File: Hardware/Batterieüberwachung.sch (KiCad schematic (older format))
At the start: 7 parts, among them Q1 BC847B_215

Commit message: Martin ist unförmig
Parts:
- Q301: renamed from Q1; value BC847B_215 -> BC847B_215-dk_Transistors-Bipolar-BJT-Single
- gave numbers to parts that had none: 4
- renumbered R4 to R301, R5 to R302
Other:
- moved on the sheet: C301, C302, R301, R302, R303, R304

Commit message: Ich hoffe wir koennen jetzt den Master mergen!
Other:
- note added: "MOSFET statt Bipolar"
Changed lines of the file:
@@
 	7400 4600 7100 4600
 Connection ~ 7100 4600
+Text Notes 5750 3700 0    20   ~ 4
+MOSFET statt Bipolar
 $EndSCHEMATC

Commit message: Zwischenspeicher Arbeit OTH
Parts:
- removed Q301: BC847B_215-dk_Transistors-Bipolar-BJT-Single, digikey-footprints:SOT-23-3, symbol E-Ink-rescue:BC847B_215-dk_Transistors-Bipolar-BJT-Single
- added Q301: 2N7000, digikey-footprints:TO-92-3, symbol E-Ink:2N7000
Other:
- note removed: "MOSFET statt Bipolar"
- moved on the sheet: R301
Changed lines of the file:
@@
 EESchema Schematic File Version 4
-EELAYER 30 0
+LIBS:E-Ink-cache
+EELAYER 29 0
 EELAYER END
 $Descr A4 11693 8268
@@
 $EndDescr
 $Comp
-L E-Ink-rescue:BC847B_215-dk_Transistors-Bipolar-BJT-Single Q?
-U 1 1 5DE4FE79
-P 5600 3900
-AR Path="/5DE4FE79" Ref="Q?"  Part="1"
-AR Path="/5DE4BC0A/5DE4FE79" Ref="Q301"  Part="1"
-F 0 "Q301" V 5827 4032 60  0000 C CNN
-F 1 "BC847B_215-dk_Transistors-Bipolar-BJT-Single" V 5906 3689 60  0001 C CNN
-F 2 "digikey-footprints:SOT-23-3" H 5800 4100 60  0001 L CNN
-F 3 "https://assets.nexperia.com/documents/data-sheet/BC847_SER.pdf" H 5800 4200 60  0001 L CNN
-F 4 "1727-2921-1-ND" H 5800 4300 60  0001 L CNN "Digi-Key_PN"
-F 5 "BC847B,215" H 5800 4400 60  0001 L CNN "MPN"
-F 6 "Discrete Semiconductor Products" H 5800 4500 60  0001 L CNN "Category"
-F 7 "Transistors - Bipolar (BJT) - Single" H 5800 4600 60  0001 L CNN "Family"
-F 8 "https://assets.nexperia.com/documents/data-sheet/BC847_SER.pdf" H 5800 4700 60  0001 L CNN "DK_Datasheet_Link"
-F 9 "/product-detail/en/nexperia-usa-inc/BC847B,215/1727-2921-1-ND/763460" H 5800 4800 60  0001 L CNN "DK_Detail_Page"
-F 10 "TRANS NPN 45V 0.1A SOT23" H 5800 4900 60  0001 L CNN "Description"
-F 11 "Nexperia USA Inc." H 5800 5000 60  0001 L CNN "Manufacturer"
-F 12 "Active" H 5800 5100 60  0001 L CNN "Status"
-	1    5600 3900
-	0    -1   -1   0
-$EndComp
-$Comp
 L power:GND #PWR?
 U 1 1 5DE4FE7F
@@
 	0    1    1    0
 $EndComp
-$Comp
-L E-Ink:4k7 R?
-U 1 1 5DE4FE8B
-P 5650 4300
-AR Path="/5DE4FE8B" Ref="R?"  Part="1"
-AR Path="/5DE4BC0A/5DE4FE8B" Ref="R301"  Part="1"
-F 0 "R301" V 5704 4328 50  0000 L CNN
-F 1 "4k7" V 5795 4328 50  0000 L CNN
-F 2 "Resistor_SMD:R_0805_2012Metric_Pad1.15x1.40mm_HandSolder" H 5700 4150 50  0001 C CNN
-F 3 "" H 5650 4350 50  0001 C CNN
-	1    5650 4300
-	0    1    1    0
-$EndComp
-Wire Wire Line
-	6100 4200 5600 4200
-Wire Wire Line
-	5600 4100 5600 4200
-Connection ~ 5600 4200
 Wire Wire Line
 	6100 3800 5800 3800
@@
 Wire Wire Line
 	3950 3950 3900 3950
-Wire Wire Line
-	5500 4600 5600 4600
 Text HLabel 3900 4100 0    50   Output ~ 10
 GPIO_Vmess
@@
 	7400 4600 7100 4600
 Connection ~ 7100 4600
-Text Notes 5750 3700 0    20   ~ 4
-MOSFET statt Bipolar
+Wire Wire Line
+	6100 4200 5700 4200
+$Comp
+L E-Ink:4k7 R?
+U 1 1 5DE4FE8B
+P 5750 4300
+AR Path="/5DE4FE8B" Ref="R?"  Part="1"
+AR Path="/5DE4BC0A/5DE4FE8B" Ref="R301"  Part="1"
+F 0 "R301" V 5804 4328 50  0000 L CNN
+F 1 "4k7" V 5895 4328 50  0000 L CNN
+F 2 "Resistor_SMD:R_0805_2012Metric_Pad1.15x1.40mm_HandSolder" H 5800 4150 50  0001 C CNN
+F 3 "" H 5750 4350 50  0001 C CNN
+	1    5750 4300
+	0    1    1    0
+$EndComp
+$Comp
+L E-Ink:2N7000 Q301
+U 1 1 5DF417CB
+P 5600 3800
+F 0 "Q301" V 5867 3800 60  0000 C CNN
+F 1 "2N7000" V 5761 3800 60  0000 C CNN
+F 2 "digikey-footprints:TO-92-3" H 5800 4000 60  0001 L CNN
+F 3 "https://www.onsemi.com/pub/Collateral/NDS7002A-D.PDF" H 5800 4100 60  0001 L CNN
+F 4 "2N7000FS-ND" H 5800 4200 60  0001 L CNN "Digi-Key_PN"
+F 5 "2N7000" H 5800 4300 60  0001 L CNN "MPN"
+F 6 "Discrete Semiconductor Products" H 5800 4400 60  0001 L CNN "Category"
+F 7 "Transistors - FETs, MOSFETs - Single" H 5800 4500 60  0001 L CNN "Family"
+F 8 "https://www.onsemi.com/pub/Collateral/NDS7002A-D.PDF" H 5800 4600 60  0001 L CNN "DK_Datasheet_Link"
+F 9 "/product-detail/en/on-semiconductor/2N7000/2N7000FS-ND/244278" H 5800 4700 60  0001 L CNN "DK_Detail_Page"
+F 10 "MOSFET N-CH 60V 200MA TO-92" H 5800 4800 60  0001 L CNN "Description"
+F 11 "ON Semiconductor" H 5800 4900 60  0001 L CNN "Manufacturer"
+F 12 "Active" H 5800 5000 60  0001 L CNN "Status"
+	1    5600 3800
+	0    -1   -1   0
+$EndComp
+Wire Wire Line
+	5700 4100 5700 4200
+Connection ~ 5700 4200
+Wire Wire Line
+	5500 4600 5700 4600
 $EndSCHEMATC

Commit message: save work at arges, finished layout and routing
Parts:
- Q301: footprint digikey-footprints:TO-92-3 -> Digikey:TO-92-3
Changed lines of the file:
@@
 EESchema Schematic File Version 4
 LIBS:E-Ink-cache
-EELAYER 29 0
+EELAYER 30 0
 EELAYER END
 $Descr A4 11693 8268
@@
 F 0 "Q301" V 5867 3800 60  0000 C CNN
 F 1 "2N7000" V 5761 3800 60  0000 C CNN
-F 2 "digikey-footprints:TO-92-3" H 5800 4000 60  0001 L CNN
+F 2 "Digikey:TO-92-3" H 5800 4000 60  0001 L CNN
 F 3 "https://www.onsemi.com/pub/Collateral/NDS7002A-D.PDF" H 5800 4100 60  0001 L CNN
 F 4 "2N7000FS-ND" H 5800 4200 60  0001 L CNN "Digi-Key_PN"

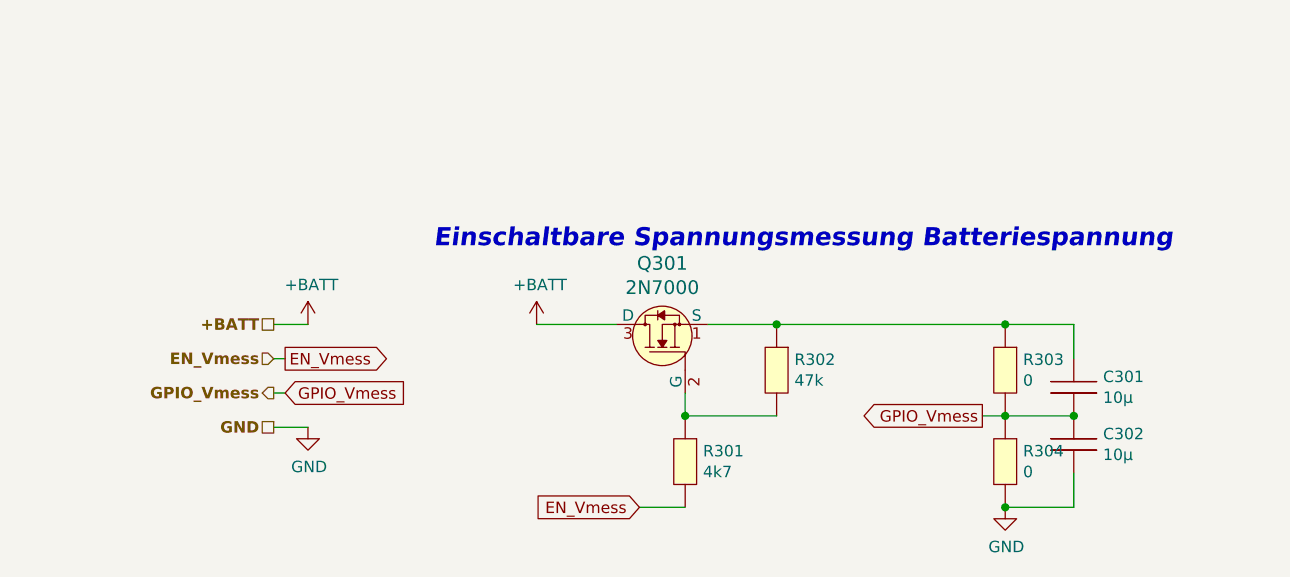
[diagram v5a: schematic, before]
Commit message: Added new MCU and redesigned schematics
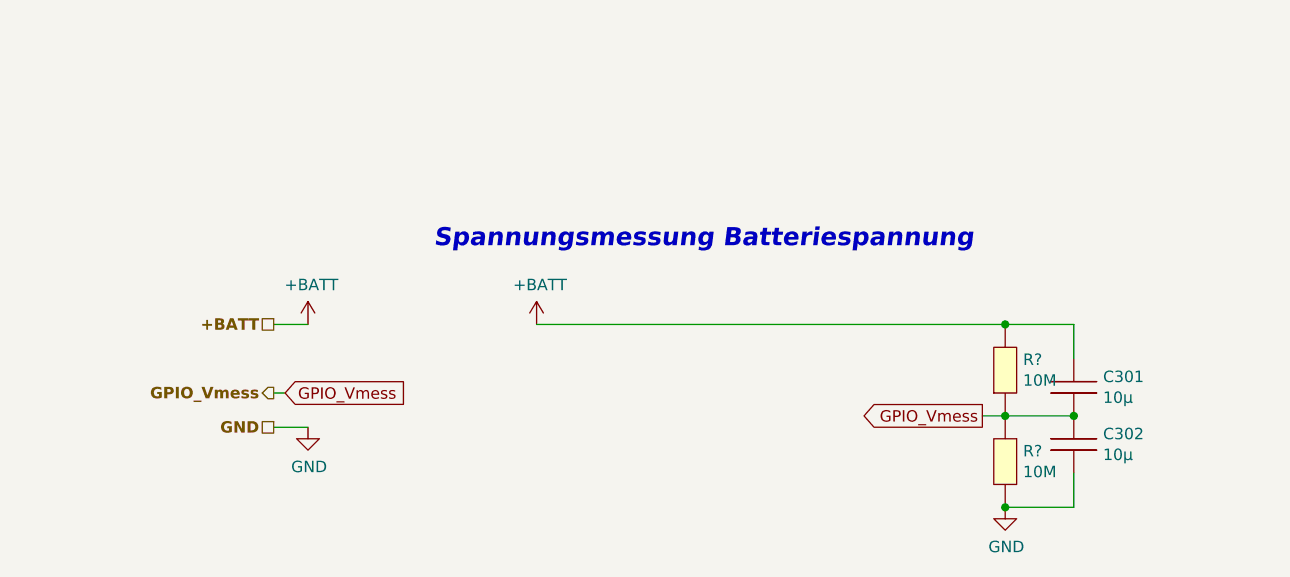
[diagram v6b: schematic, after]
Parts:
- removed Q301: 2N7000, Digikey:TO-92-3, symbol E-Ink:2N7000
- removed R301: 4k7, Resistor_SMD:R_0805_2012Metric_Pad1.15x1.40mm_HandSolder, symbol E-Ink:4k7
- removed R302: 47k, Resistor_SMD:R_0805_2012Metric_Pad1.15x1.40mm_HandSolder, symbol E-Ink:47k
- removed R303, R304: 0, Resistor_SMD:R_0805_2012Metric_Pad1.15x1.40mm_HandSolder, symbol E-Ink:0
- added R? (x2): 10M, Resistor_SMD:R_0805_2012Metric_Pad1.15x1.40mm_HandSolder, symbol E-Ink:10M
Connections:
- net +BATT: now also C301.1, R?.2
- net GND: now also R?.2
- net GPIO_Vmess: now also R?.1, R?.1
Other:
- note added: "Spannungsmessung Batteriespannung\n\n"
- note removed: "Einschaltbare Spannungsmessung Batteriespannung\n\n"
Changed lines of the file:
@@
 EESchema Schematic File Version 4
-LIBS:E-Ink-cache
 EELAYER 30 0
 EELAYER END
@@
 	1    0    0    -1
 $EndComp
-$Comp
-L E-Ink:47k R?
-U 1 1 5DE4FE85
-P 6150 3900
-AR Path="/5DE4FE85" Ref="R?"  Part="1"
-AR Path="/5DE4BC0A/5DE4FE85" Ref="R302"  Part="1"
-F 0 "R302" V 6204 3928 50  0000 L CNN
-F 1 "47k" V 6295 3928 50  0000 L CNN
-F 2 "Resistor_SMD:R_0805_2012Metric_Pad1.15x1.40mm_HandSolder" H 6200 3750 50  0001 C CNN
-F 3 "" H 6150 3950 50  0001 C CNN
-	1    6150 3900
-	0    1    1    0
-$EndComp
-Wire Wire Line
-	6100 3800 5800 3800
-Connection ~ 6100 3800
 Text GLabel 7000 4200 0    50   Output ~ 0
 GPIO_Vmess
-Wire Wire Line
-	6100 3800 7100 3800
-Text GLabel 5500 4600 0    50   Input ~ 0
-EN_Vmess
 $Comp
 L power:+BATT #PWR?
@@
 	1    0    0    -1
 $EndComp
-Wire Wire Line
-	5050 3800 5400 3800
 Text Notes 4600 3600 0    79   Italic 16
-Einschaltbare Spannungsmessung Batteriespannung\n\n
-Text HLabel 3900 3950 0    50   Input ~ 10
-EN_Vmess
+Spannungsmessung Batteriespannung\n\n
 Text HLabel 3900 3800 0    50   UnSpc ~ 10
 +BATT
@@
 Wire Wire Line
 	4050 3800 3900 3800
-Text GLabel 3950 3950 2    50   Output ~ 0
-EN_Vmess
-Wire Wire Line
-	3950 3950 3900 3950
 Text HLabel 3900 4100 0    50   Output ~ 10
 GPIO_Vmess
@@
 	4050 4250 3900 4250
 $Comp
-L E-Ink:0 R303
-U 1 1 5DEEEA28
-P 7150 3900
-F 0 "R303" V 7204 3928 50  0000 L CNN
-F 1 "0" V 7295 3928 50  0000 L CNN
-F 2 "Resistor_SMD:R_0805_2012Metric_Pad1.15x1.40mm_HandSolder" H 7200 3750 50  0001 C CNN
-F 3 "" H 7150 3950 50  0001 C CNN
-	1    7150 3900
-	0    1    1    0
-$EndComp
-$Comp
-L E-Ink:0 R304
-U 1 1 5DEEF0E3
-P 7150 4300
-F 0 "R304" V 7204 4328 50  0000 L CNN
-F 1 "0" V 7295 4328 50  0000 L CNN
-F 2 "Resistor_SMD:R_0805_2012Metric_Pad1.15x1.40mm_HandSolder" H 7200 4150 50  0001 C CNN
-F 3 "" H 7150 4350 50  0001 C CNN
-	1    7150 4300
-	0    1    1    0
-$EndComp
-Wire Wire Line
-	7000 4200 7100 4200
-Connection ~ 7100 4200
-$Comp
 L E-Ink:10µ C301
 U 1 1 5DEF06A2
@@
 	0    1    1    0
 $EndComp
-Wire Wire Line
-	7400 4200 7100 4200
 Connection ~ 7400 4200
 Wire Wire Line
 	7400 3950 7400 3800
 Wire Wire Line
-	7400 3800 7100 3800
-Connection ~ 7100 3800
-Wire Wire Line
 	7400 4450 7400 4600
 Wire Wire Line
 	7400 4600 7100 4600
-Connection ~ 7100 4600
 Wire Wire Line
-	6100 4200 5700 4200
+	5050 3800 7100 3800
+Wire Wire Line
+	7000 4200 7100 4200
 $Comp
-L E-Ink:4k7 R?
-U 1 1 5DE4FE8B
-P 5750 4300
-AR Path="/5DE4FE8B" Ref="R?"  Part="1"
-AR Path="/5DE4BC0A/5DE4FE8B" Ref="R301"  Part="1"
-F 0 "R301" V 5804 4328 50  0000 L CNN
-F 1 "4k7" V 5895 4328 50  0000 L CNN
-F 2 "Resistor_SMD:R_0805_2012Metric_Pad1.15x1.40mm_HandSolder" H 5800 4150 50  0001 C CNN
-F 3 "" H 5750 4350 50  0001 C CNN
-	1    5750 4300
+L E-Ink:10M R?
+U 1 1 5F96A47F
+P 7000 4000
+F 0 "R?" V 7046 3822 50  0000 R CNN
+F 1 "10M" V 6955 3822 50  0000 R CNN
+F 2 "Resistor_SMD:R_0805_2012Metric_Pad1.15x1.40mm_HandSolder" H 6900 3800 50  0001 C CNN
+F 3 "" H 6900 4000 50  0001 C CNN
+	1    7000 4000
+	0    -1   -1   0
+$EndComp
+Connection ~ 7100 4200
+Wire Wire Line
+	7100 4200 7400 4200
+Connection ~ 7100 3800
+Wire Wire Line
+	7100 3800 7400 3800
+$Comp
+L E-Ink:10M R?
+U 1 1 5F96AD7C
+P 7200 4400
+F 0 "R?" V 7154 4378 50  0000 L CNN
+F 1 "10M" V 7245 4378 50  0000 L CNN
+F 2 "Resistor_SMD:R_0805_2012Metric_Pad1.15x1.40mm_HandSolder" H 7100 4200 50  0001 C CNN
+F 3 "" H 7100 4400 50  0001 C CNN
+	1    7200 4400
 	0    1    1    0
 $EndComp
-$Comp
-L E-Ink:2N7000 Q301
-U 1 1 5DF417CB
-P 5600 3800
-F 0 "Q301" V 5867 3800 60  0000 C CNN
-F 1 "2N7000" V 5761 3800 60  0000 C CNN
-F 2 "Digikey:TO-92-3" H 5800 4000 60  0001 L CNN
-F 3 "https://www.onsemi.com/pub/Collateral/NDS7002A-D.PDF" H 5800 4100 60  0001 L CNN
-F 4 "2N7000FS-ND" H 5800 4200 60  0001 L CNN "Digi-Key_PN"
-F 5 "2N7000" H 5800 4300 60  0001 L CNN "MPN"
-F 6 "Discrete Semiconductor Products" H 5800 4400 60  0001 L CNN "Category"
-F 7 "Transistors - FETs, MOSFETs - Single" H 5800 4500 60  0001 L CNN "Family"
-F 8 "https://www.onsemi.com/pub/Collateral/NDS7002A-D.PDF" H 5800 4600 60  0001 L CNN "DK_Datasheet_Link"
-F 9 "/product-detail/en/on-semiconductor/2N7000/2N7000FS-ND/244278" H 5800 4700 60  0001 L CNN "DK_Detail_Page"
-F 10 "MOSFET N-CH 60V 200MA TO-92" H 5800 4800 60  0001 L CNN "Description"
-F 11 "ON Semiconductor" H 5800 4900 60  0001 L CNN "Manufacturer"
-F 12 "Active" H 5800 5000 60  0001 L CNN "Status"
-	1    5600 3800
-	0    -1   -1   0
-$EndComp
-Wire Wire Line
-	5700 4100 5700 4200
-Connection ~ 5700 4200
-Wire Wire Line
-	5500 4600 5700 4600
+Connection ~ 7100 4600
 $EndSCHEMATC

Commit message: finished PCB, Thursday Review with Lukas
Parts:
- R301, R302: renamed from R?; footprint Resistor_SMD:R_0805_2012Metric_Pad1.15x1.40mm_HandSolder -> Resistor_SMD:R_0805_2012Metric_Pad1.20x1.40mm_HandSolder
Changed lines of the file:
@@
 	7000 4200 7100 4200
 $Comp
-L E-Ink:10M R?
+L E-Ink:10M R301
 U 1 1 5F96A47F
 P 7000 4000
-F 0 "R?" V 7046 3822 50  0000 R CNN
+F 0 "R301" V 7046 3822 50  0000 R CNN
 F 1 "10M" V 6955 3822 50  0000 R CNN
-F 2 "Resistor_SMD:R_0805_2012Metric_Pad1.15x1.40mm_HandSolder" H 6900 3800 50  0001 C CNN
+F 2 "Resistor_SMD:R_0805_2012Metric_Pad1.20x1.40mm_HandSolder" H 6900 3800 50  0001 C CNN
 F 3 "" H 6900 4000 50  0001 C CNN
 	1    7000 4000
@@
 	7100 3800 7400 3800
 $Comp
-L E-Ink:10M R?
+L E-Ink:10M R302
 U 1 1 5F96AD7C
 P 7200 4400
-F 0 "R?" V 7154 4378 50  0000 L CNN
+F 0 "R302" V 7154 4378 50  0000 L CNN
 F 1 "10M" V 7245 4378 50  0000 L CNN
-F 2 "Resistor_SMD:R_0805_2012Metric_Pad1.15x1.40mm_HandSolder" H 7100 4200 50  0001 C CNN
+F 2 "Resistor_SMD:R_0805_2012Metric_Pad1.20x1.40mm_HandSolder" H 7100 4200 50  0001 C CNN
 F 3 "" H 7100 4400 50  0001 C CNN
 	1    7200 4400
